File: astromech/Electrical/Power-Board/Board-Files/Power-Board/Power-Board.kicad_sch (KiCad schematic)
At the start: 74 parts, among them J1 BAT_IN_SCREW, J10 HEAD_MOT, J2 BAT_IN_HOLE, J5 E_STOP, J6 CTRL_BRD, J7 JETSON, J8 L_DRIVE, J9 R_DRIVE, Q1 Q_NMOS_DSG, Q2 Q_NMOS_DSG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

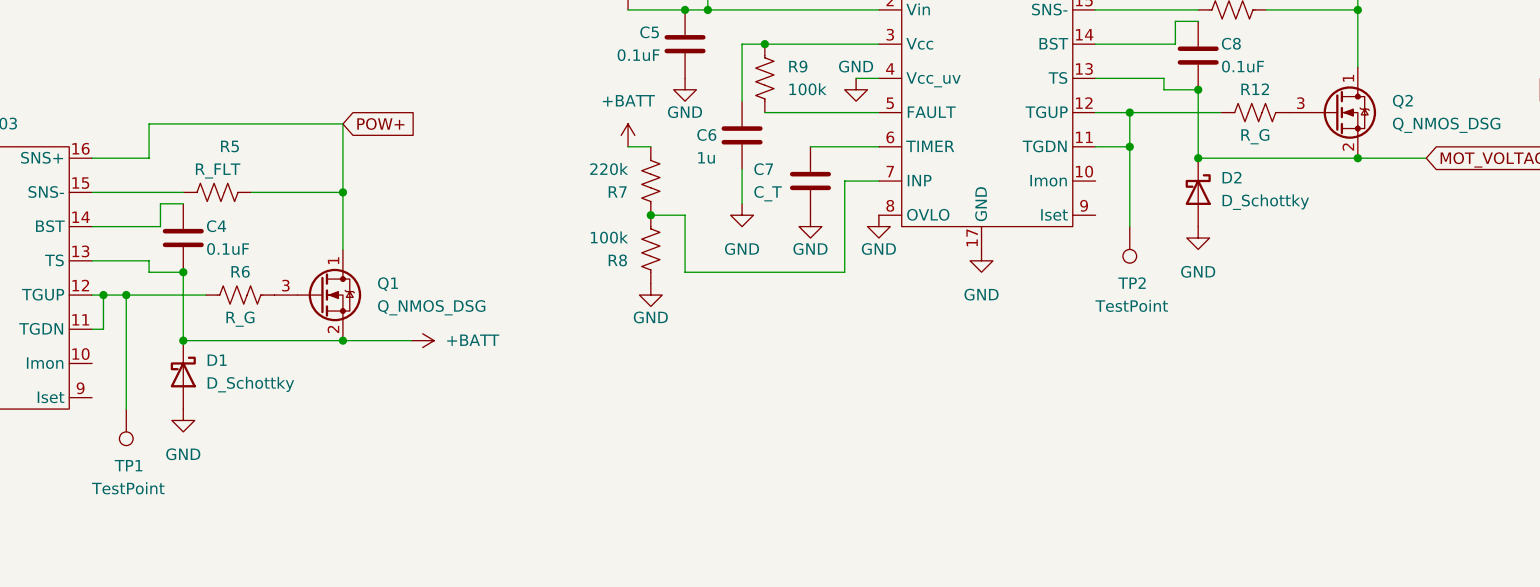
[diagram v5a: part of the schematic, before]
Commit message: Assigned shottky diode footprints
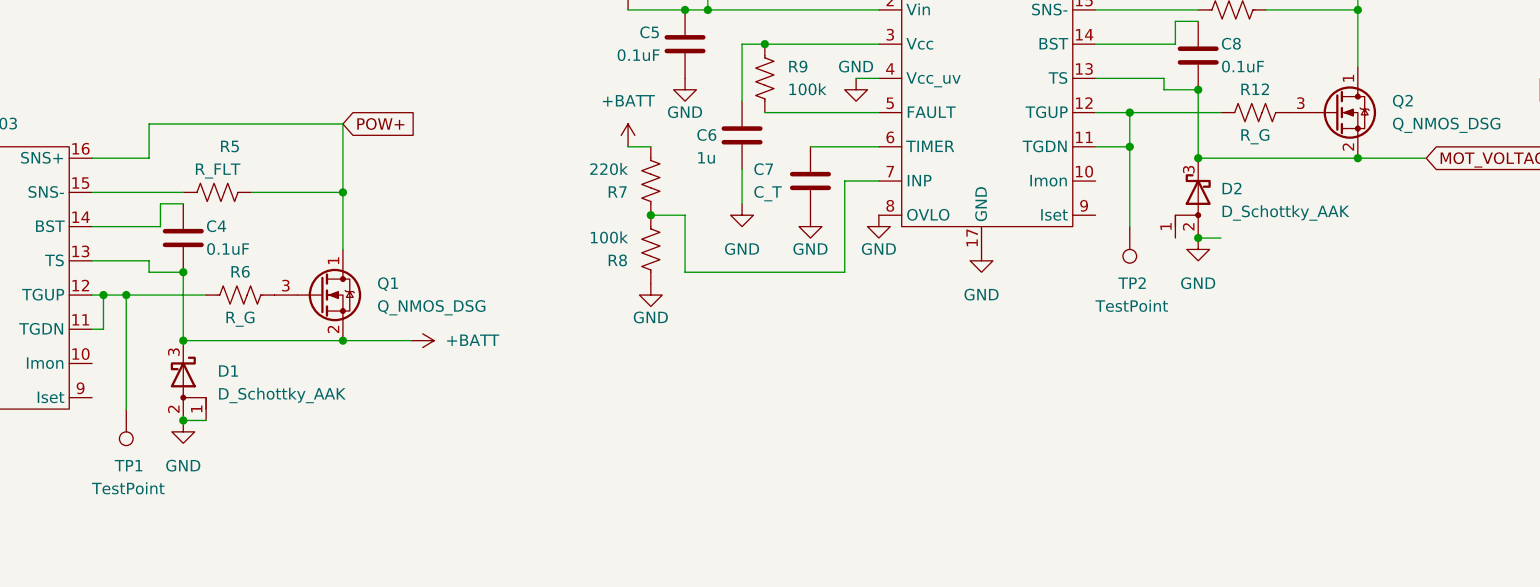
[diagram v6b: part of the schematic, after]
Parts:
- removed D1, D2: D_Schottky, symbol Device:D_Schottky
- added D1, D2: D_Schottky_AAK, Package_TO_SOT_SMD:TO-277A, symbol Device:D_Schottky_AAK
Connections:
- net +BATT: now also D1.3 (K)
- net GND: now also D1.1 (A), D1.2 (A), D2.2 (A)
- net MOT_VOLTAGE: now also D2.3 (K)

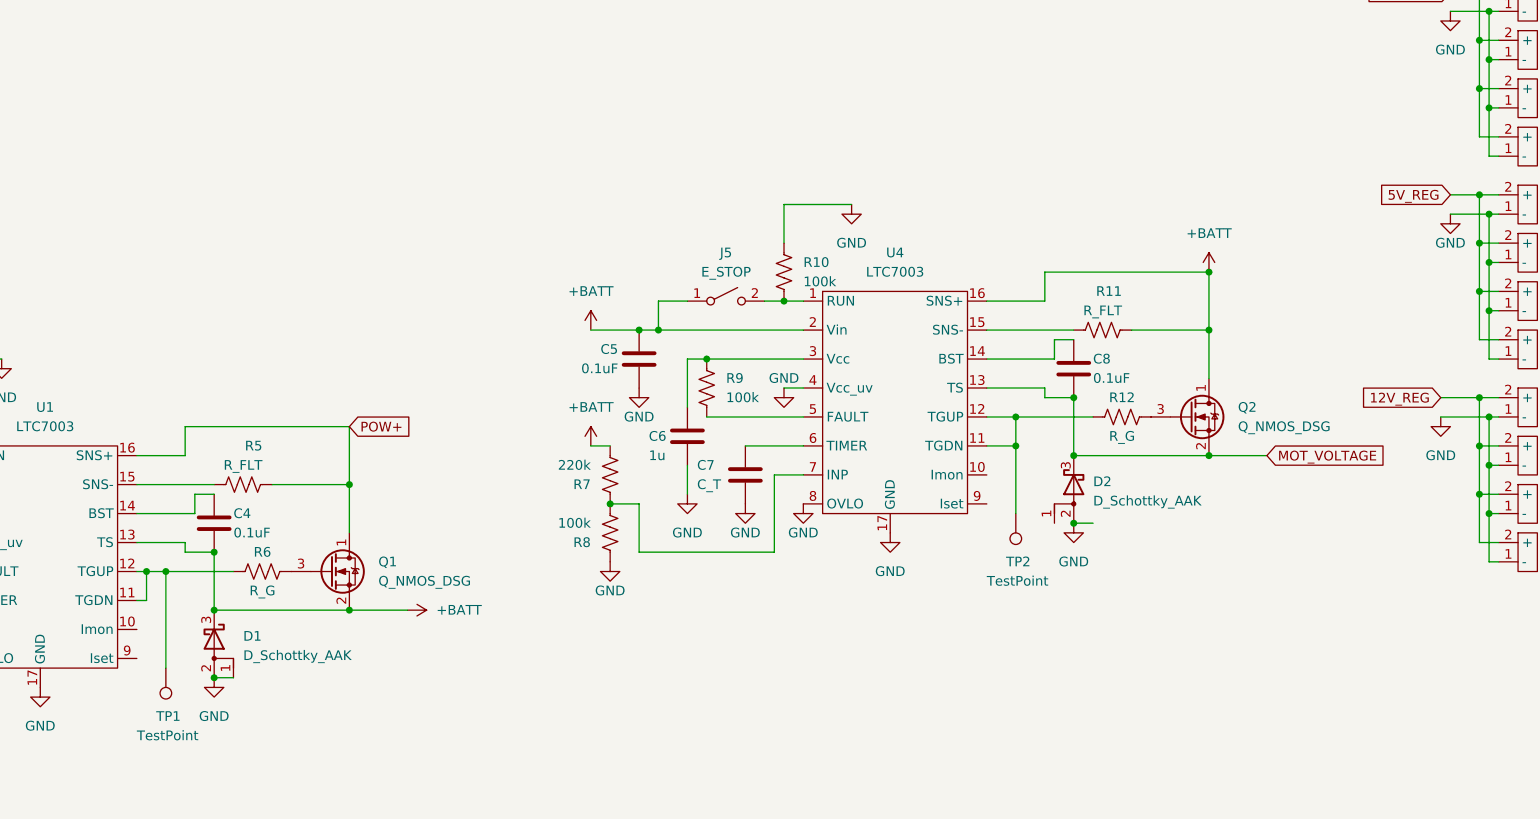
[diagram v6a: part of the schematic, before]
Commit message: added LTC7003 current inrush limiting
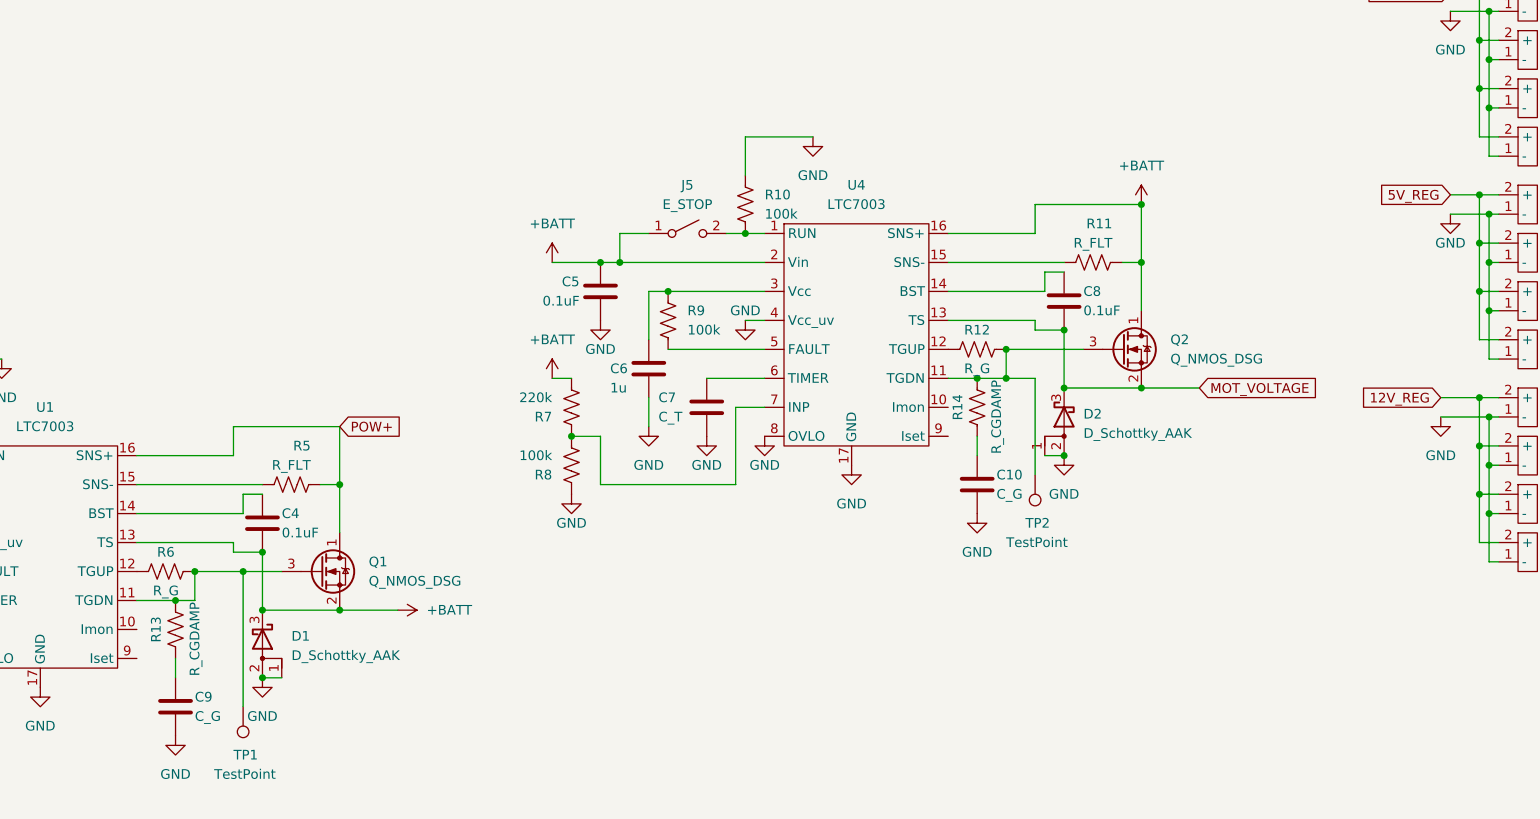
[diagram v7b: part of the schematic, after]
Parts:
- added C10, C9: C_G, Capacitor_SMD:C_1206_3216Metric_Pad1.33x1.80mm_HandSolder, symbol Device:C
- added R13, R14: R_CGDAMP, Resistor_SMD:R_1206_3216Metric_Pad1.30x1.75mm_HandSolder, symbol Device:R_US
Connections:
- net GND: now also D2.1 (A), C10.2, C9.2
- net at TP2.1, U4.11 (TGDN): now also Q2.3 (G), R12.2, R14.2; no longer R12.1, U4.12 (TGUP)
- net at R6.1, U1.12 (TGUP): no longer TP1.1, U1.11 (TGDN)
- net at Q1.3 (G), R6.2: now also TP1.1, U1.11 (TGDN), R13.2
- new net: R12.1, U4.12 (TGUP)
- new net: C10.1, R14.1
- new net: C9.1, R13.1
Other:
- moved on the sheet: C4, C5, C6, C7, C8, D1, D2, J5, Q1, Q2, R10, R11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

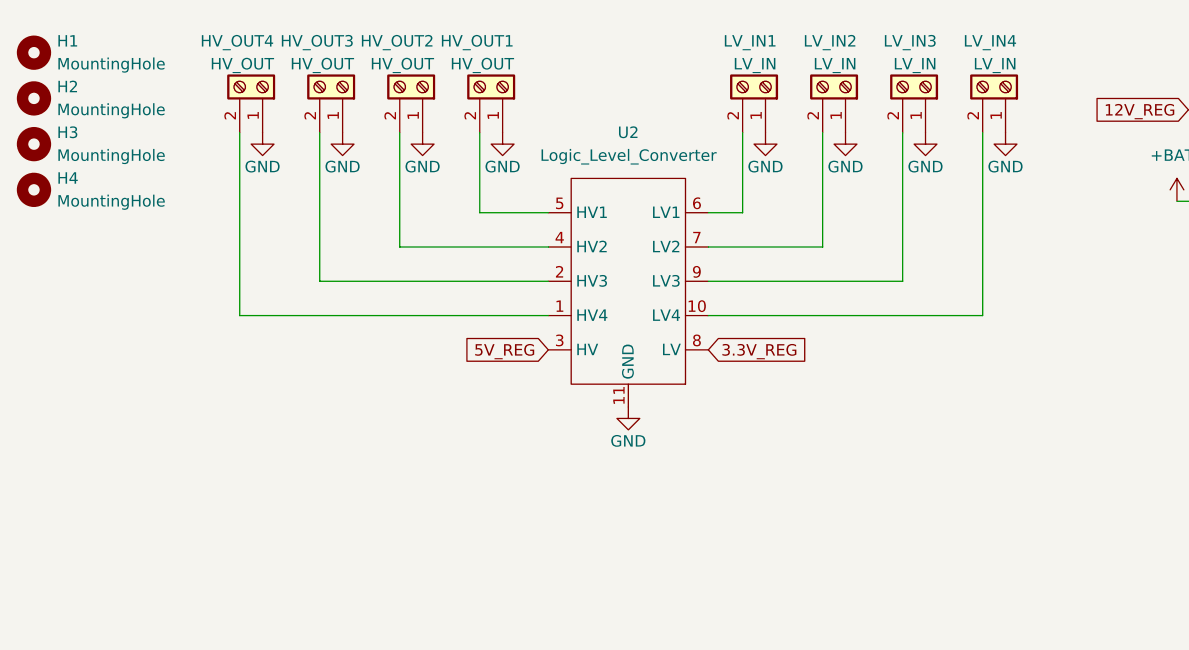
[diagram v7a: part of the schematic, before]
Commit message: Modified level converter connections
Made to fit NEO encoder connection order
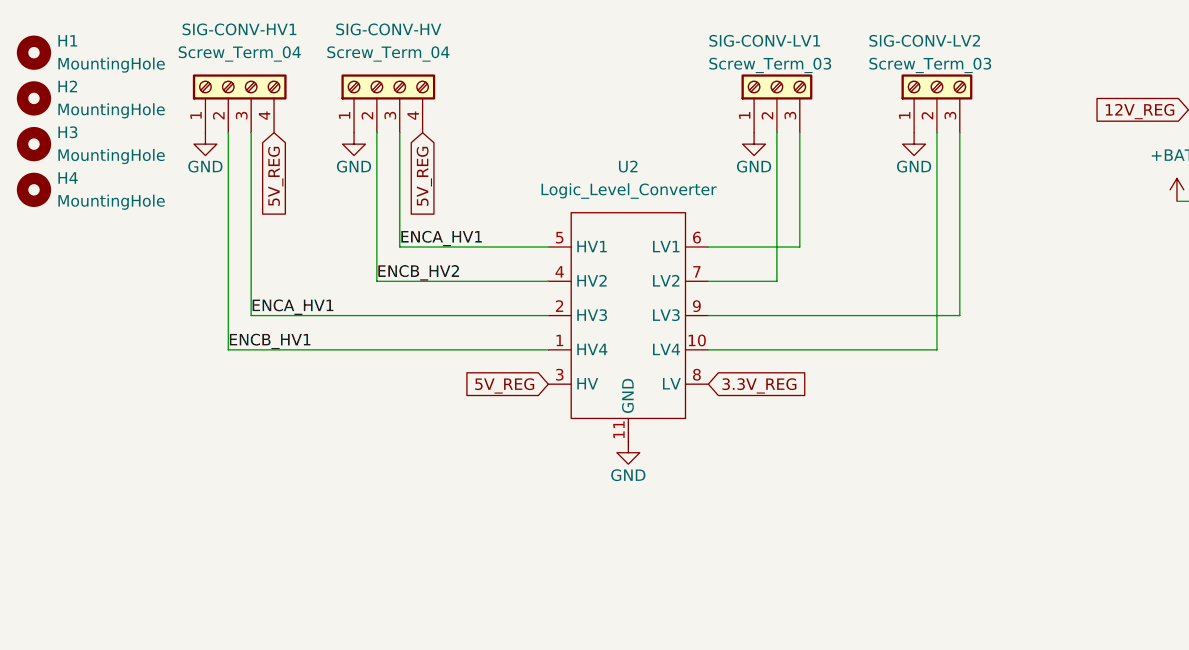
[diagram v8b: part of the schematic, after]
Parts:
- removed HV_OUT1, HV_OUT2, HV_OUT3, HV_OUT4: HV_OUT, astromech-footprints:Phoenix-1935161, symbol Connector:Screw_Terminal_01x02
- removed LV_IN1, LV_IN2, LV_IN3, LV_IN4: LV_IN, astromech-footprints:Phoenix-1935161, symbol Connector:Screw_Terminal_01x02
- added SIG-CONV-HV, SIG-CONV-HV1: Screw_Term_04, symbol Connector:Screw_Terminal_01x04
- added SIG-CONV-LV1, SIG-CONV-LV2: Screw_Term_03, symbol Connector:Screw_Terminal_01x03
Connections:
- net 5V_REG: now also SIG-CONV-HV.4 (Pin_4), SIG-CONV-HV1.4 (Pin_4)
- net GND: now also SIG-CONV-HV.1 (Pin_1), SIG-CONV-HV1.1 (Pin_1), SIG-CONV-LV1.1 (Pin_1), SIG-CONV-LV2.1 (Pin_1)
- net ENCB_HV2: now reaches U2.4 (HV2)
- net ENCB_HV2: now also SIG-CONV-HV.2 (Pin_2)
- net at U2.6 (LV1): now also SIG-CONV-LV1.3 (Pin_3)
- net ENCB_HV1: now reaches U2.1 (HV4)
- net ENCB_HV1: now also SIG-CONV-HV1.2 (Pin_2)
- net at U2.10 (LV4): now also SIG-CONV-LV2.2 (Pin_2)
- net ENCA_HV1: now reaches U2.2 (HV3)
- net ENCA_HV1: now also U2.5 (HV1), SIG-CONV-HV.3 (Pin_3), SIG-CONV-HV1.3 (Pin_3)
- net at U2.7 (LV2): now also SIG-CONV-LV1.2 (Pin_2)
- net at U2.9 (LV3): now also SIG-CONV-LV2.3 (Pin_3)
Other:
- moved on the sheet: U2
